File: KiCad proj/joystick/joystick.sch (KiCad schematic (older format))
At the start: 33 parts, among them J1 Joystic_conn, J2 USB_conn, J3 Keyboard_conn, J4 SWD, Q1 Q_PNP_BEC, U1 STM32F103C8Tx, U2 NCP500SN33T1, Y1 16MHz

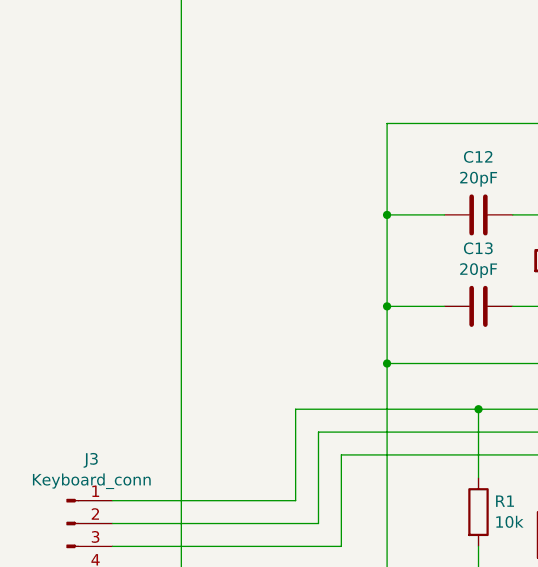
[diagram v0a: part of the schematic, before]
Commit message: Add labels to keyboard pins
Add labels to keyboard pins in order to have explicit key->port B pins
mapping
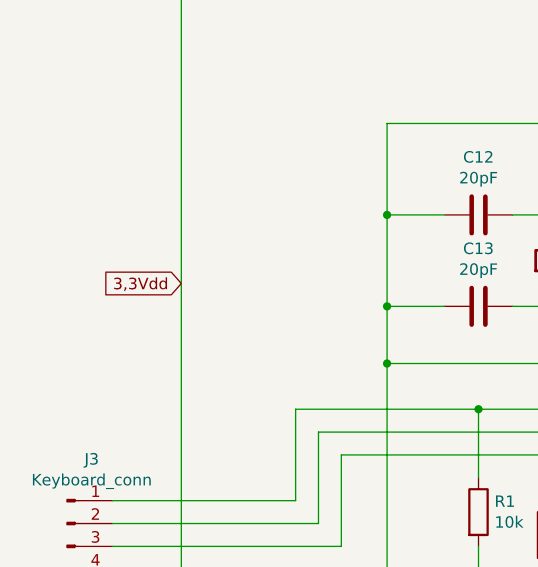
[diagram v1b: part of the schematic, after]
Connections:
- net 3.3 renamed 3,3Vdd
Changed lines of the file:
@@
 Wire Wire Line
 	6700 4250 6700 4550
+Text GLabel 2600 3100 0    50   Input ~ 0
+3,3Vdd
 $EndSCHEMATC

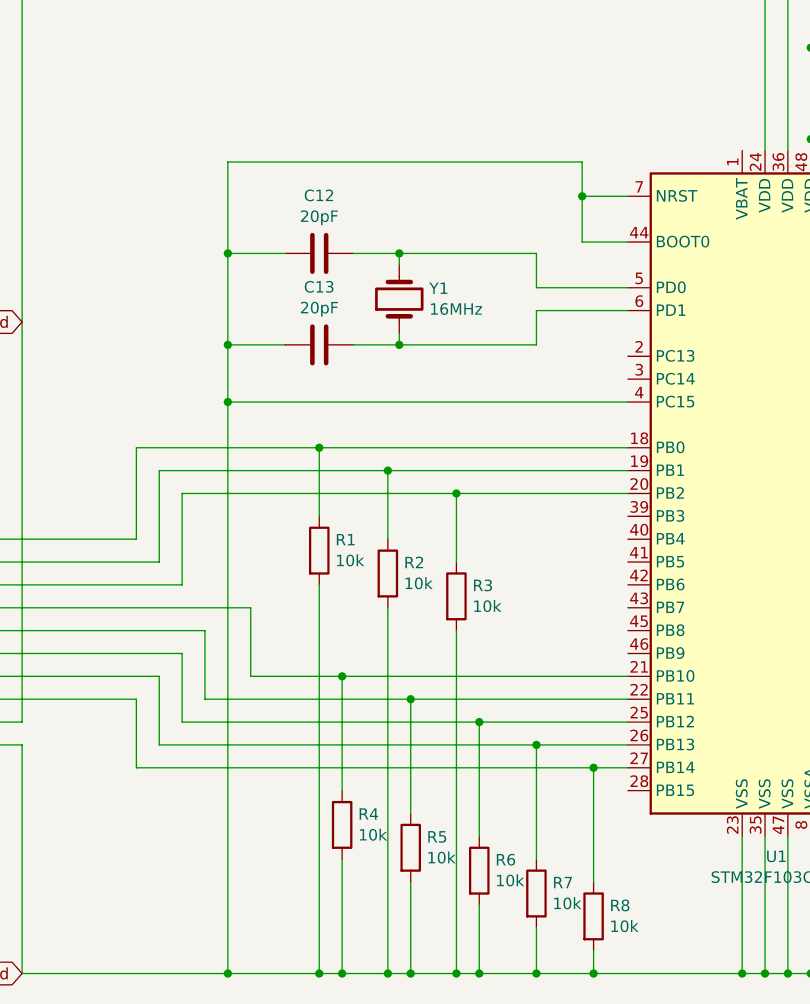
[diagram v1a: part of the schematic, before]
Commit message: Add new joystick shcematics
Add schematics for keyboard and jouystick adaptors
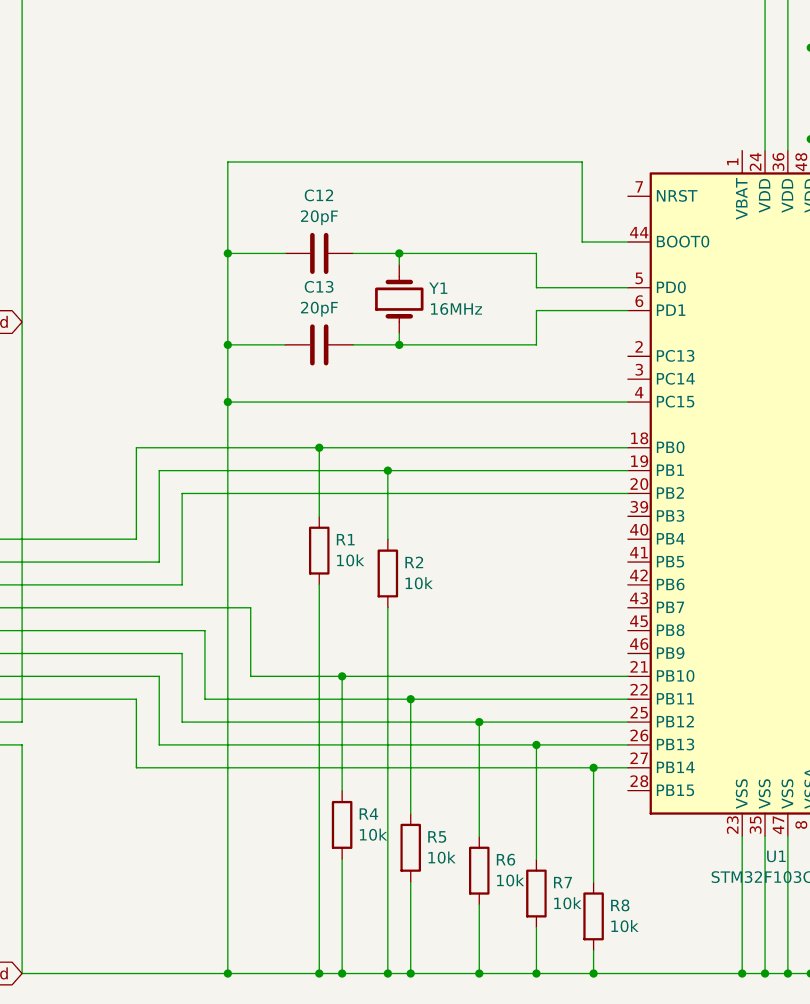
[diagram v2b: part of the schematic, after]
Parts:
- removed R3: 10k, Resistor_SMD:R_0201_0603Metric_Pad0.64x0.40mm_HandSolder, symbol Device:R
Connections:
- net Gnd: no longer U1.7 (NRST)
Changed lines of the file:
@@
 USB_DP
 Wire Wire Line
-	4500 4150 4500 3850
-Wire Wire Line
 	4200 4050 4200 3750
 Wire Wire Line
 	3900 3650 3900 3950
-$Comp
-L Device:R R3
-U 1 1 60CC23D9
-P 4500 4300
-F 0 "R3" H 4570 4346 50  0000 L CNN
-F 1 "10k" H 4570 4255 50  0000 L CNN
-F 2 "Resistor_SMD:R_0201_0603Metric_Pad0.64x0.40mm_HandSolder" V 4430 4300 50  0001 C CNN
-F 3 "~" H 4500 4300 50  0001 C CNN
-	1    4500 4300
-	1    0    0    -1
-$EndComp
 $Comp
 L Device:R R2
@@
 	4300 5250 4300 4750
 Wire Wire Line
-	4500 4450 4500 5950
-Wire Wire Line
 	4300 5550 4300 5950
 Wire Wire Line
@@
 Wire Wire Line
 	4300 4750 5250 4750
-Wire Wire Line
-	4300 5950 4500 5950
 Connection ~ 3900 3650
 Wire Wire Line
@@
 Wire Wire Line
 	3900 5950 4000 5950
-Connection ~ 4500 3850
-Connection ~ 4500 5950
-Wire Wire Line
-	4500 3850 5250 3850
-Wire Wire Line
-	4500 5950 4600 5950
 Connection ~ 4600 4850
 Connection ~ 4600 5950
@@
 	3300 4250 3300 3850
 Wire Wire Line
-	3300 3850 4500 3850
-Wire Wire Line
 	2300 4350 3600 4350
 Wire Wire Line
@@
 $EndComp
 Wire Wire Line
-	5050 2550 5050 2750
-Wire Wire Line
-	5050 2550 5250 2550
-Wire Wire Line
 	3500 2400 5050 2400
-Wire Wire Line
-	5050 2400 5050 2550
-Connection ~ 5050 2550
 Wire Wire Line
 	6750 1250 6750 1900
@@
 Text GLabel 2600 3100 0    50   Input ~ 0
 3,3Vdd
+Wire Wire Line
+	3300 3850 5250 3850
+Wire Wire Line
+	4300 5950 4600 5950
+Wire Wire Line
+	5050 2400 5050 2750
 $EndSCHEMATC
